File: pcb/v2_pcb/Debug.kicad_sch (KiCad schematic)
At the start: 2 parts, among them J1 Conn_ARM_SWD_TagConnect_TC203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

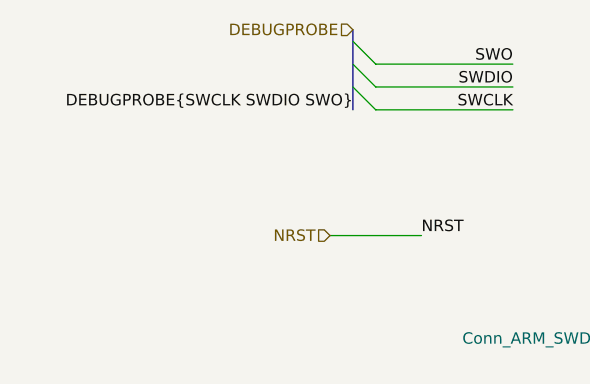
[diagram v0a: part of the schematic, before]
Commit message: done with max17320
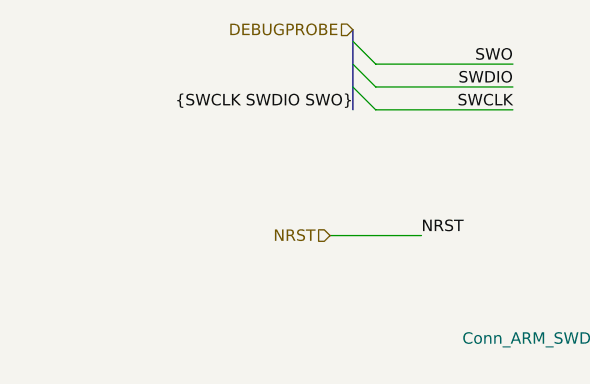
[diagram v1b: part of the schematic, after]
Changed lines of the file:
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@@
 		)
 	)
-	(label "DEBUGPROBE{SWCLK SWDIO SWO}"
+	(label "{SWCLK SWDIO SWO}"
 		(at 91.44 73.66 180)
 		(effects

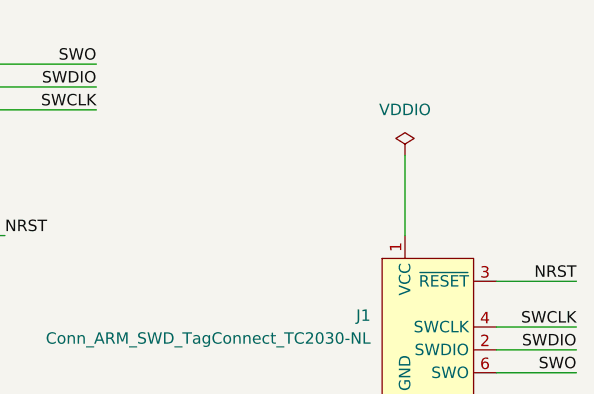
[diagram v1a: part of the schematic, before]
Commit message: add rpls for 1v8, 5v
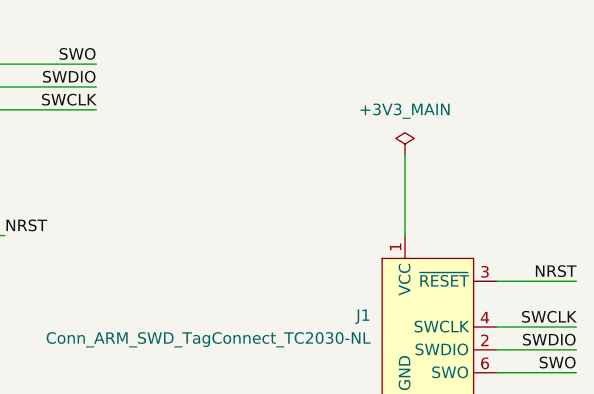
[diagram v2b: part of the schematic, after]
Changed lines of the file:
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@@
 			)
 		)
-		(property "Value" "VDDIO"
+		(property "Value" "+3V3_MAIN"
 			(at 143.51 73.66 0)
 			(show_name no)

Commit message: pcb done
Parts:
- added R327: 10k, Resistor_SMD:R_0402_1005Metric, symbol Device:R_Small_US
- added SW301: DEV BOOT, Button_Switch_SMD:SW_Push_1P1T_NO_CK_KMR2, symbol Switch:SW_Push
- added TP300: DEV_BOOT, TestPoint:TestPoint_Plated_Hole_D2.0mm, symbol Connector:TestPoint
- C1: footprint (none) -> Capacitor_SMD:C_0402_1005Metric
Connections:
- net GND: now also J1.5 (GND), R327.2
- net +3V3_MAIN: now reaches C1.1
- net +3V3_MAIN: now also J1.1 (VCC), SW301.1; no longer J1.5 (GND)
- new net DEV_BOOT: R327.1, SW301.2, TP300.1
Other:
- note added: "BOOT1 / DEV_BOOT (MCU PA6/P8) is sampled during reset; assert high only for development boot."
- note added: "Boot truth table (AN5967 Rev.4): BOOT1=1: development boot (BOOT0 ignored) BOOT1=0, BOOT0=0: Flash-memory boot BOOT1=0, BOOT0=1: serial boot"
- moved on the sheet: J1

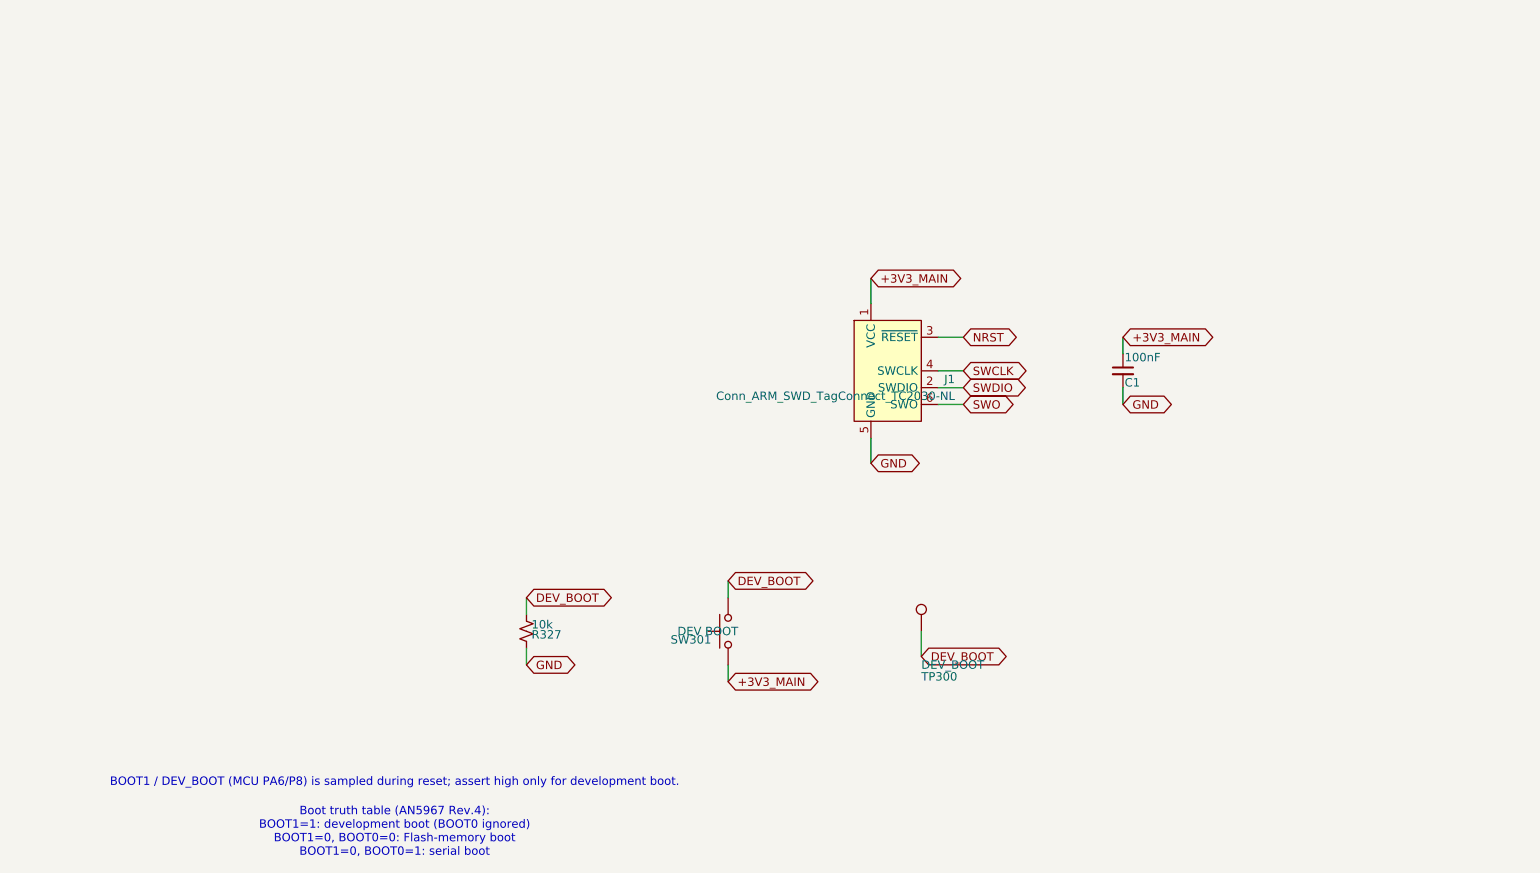
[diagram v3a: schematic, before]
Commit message: switch mosfets
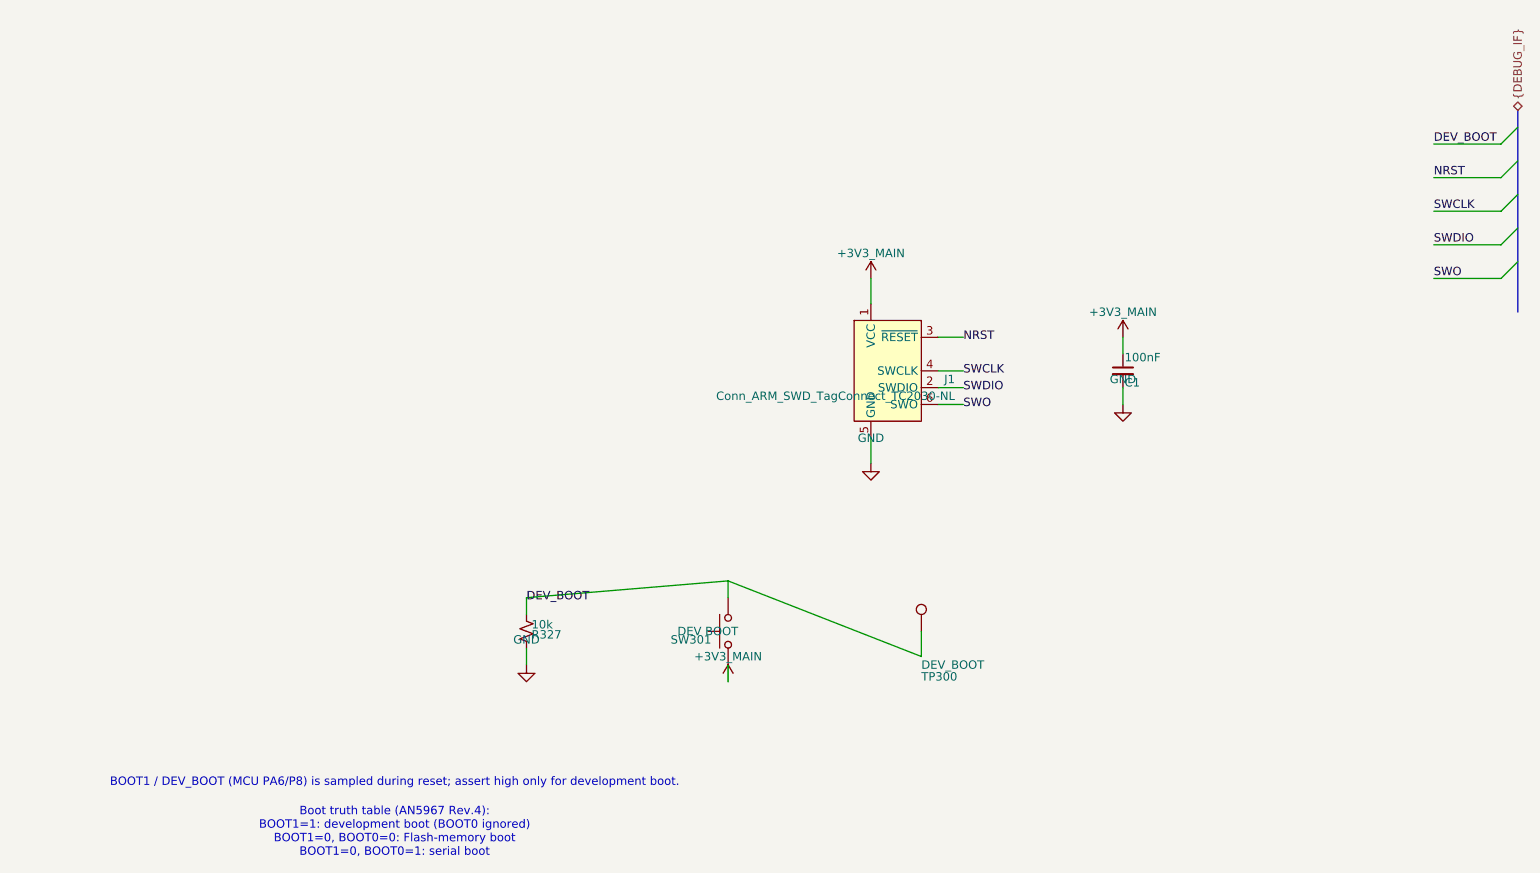
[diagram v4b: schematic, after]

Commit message: power and debug cleanup
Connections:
- net +3V3_MAIN: now also SW301.2; no longer SW301.1
- net DEV_BOOT: now also SW301.1; no longer SW301.2
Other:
- moved on the sheet: C1, R327, SW301, TP300

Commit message: minor fixes
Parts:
- C1: value 100nF -> 100nF 50V X7R; Dielectric (none) -> X7R; MPN (none) -> CGA2B3X7R1H104K050BE; Manufacturer (none) -> TDK; Qualification (none) -> AEC-Q200; Termination (none) -> Soft termination; Tolerance (none) -> ±10%; Voltage (none) -> 50 VDC
- R327: MPN RC0402FR-0710KL -> CRCW040210K0FKED; Manufacturer Yageo -> Vishay; Power (none) -> 0.063 W; Qualification (none) -> AEC-Q200; TCR (none) -> ±100 ppm/K; Tolerance (none) -> ±1%
- SW301: value DEV BOOT -> KMR223NG ULC LFG; Contact (none) -> Gold ULC; 1 µA minimum at 1.8 V; MPN KMR221GLFS -> Y78B22324FP; Manufacturer C&K -> Littelfuse (C&K); Operating_Temperature (none) -> -40 to +125 °C
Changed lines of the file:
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@@
 		)
 	)
-	(label "NRST"
+	(global_label "NRST"
 		(at 212.09 66.04 0)
 		(effects
@@
 		)
 	)
-	(label "NRST"
+	(global_label "NRST"
 		(at 140.97 90.17 0)
 		(effects
@@
 			)
 		)
-		(property "Value" "DEV BOOT"
+		(property "Value" "KMR223NG ULC LFG"
 			(at 120.65 123.19 0)
 			(show_name no)
@@
 			)
 		)
-		(property "Datasheet" ""
+		(property "Datasheet" "https://www.littelfuse.com/assetdocs/littelfuse-ck-tactile-kmr2-series-datasheet?assetguid=f782bfc7-b600-4ab5-8c8d-a2a094a642e3"
 			(at 120.65 127 0)
 			(show_name no)
@@
 			)
 		)
-		(property "MPN" "KMR221GLFS"
+		(property "MPN" "Y78B22324FP"
 			(at 123.19 132.0799 0)
 			(hide yes)
@@
 			)
 		)
-		(property "Manufacturer" "C&K"
+		(property "Manufacturer" "Littelfuse (C&K)"
 			(at 123.19 132.0799 0)
 			(hide yes)
@@
 			)
 		)
+    (property "Contact" "Gold ULC; 1 µA minimum at 1.8 V" (at 120.65 127.0 0)
+      (effects (font (size 1.27 1.27)) (hide yes))
+    )
+    (property "Operating_Temperature" "-40 to +125 °C" (at 120.65 127.0 0)
+      (effects (font (size 1.27 1.27)) (hide yes))
+    )
 		(pin "1"
 		)
@@
 		(in_bom no)
 		(on_board yes)
-		(in_pos_files yes)
+		(in_pos_files no)
 		(dnp no)
 		(property "Reference" "J1"
@@
 			)
 		)
-		(property "Datasheet" "https://www.yageo.com/upload/media/product/productsearch/datasheet/rchip/PYu-RC_Group_51_RoHS_L_12.pdf"
+		(property "Datasheet" "https://www.vishay.com/docs/20035/dcrcwe3.pdf"
 			(at 106.68 132.08 0)
 			(hide yes)
@@
 			)
 		)
-		(property "MPN" "RC0402FR-0710KL"
+		(property "MPN" "CRCW040210K0FKED"
 			(at 109.22 137.1599 0)
 			(hide yes)
@@
 			)
 		)
-		(property "Manufacturer" "Yageo"
+		(property "Manufacturer" "Vishay"
 			(at 109.22 137.1599 0)
 			(hide yes)
@@
 			)
 		)
+    (property "Tolerance" "±1%" (at 106.68 132.08 0)
+      (effects (font (size 1.27 1.27)) (hide yes))
+    )
+    (property "Power" "0.063 W" (at 106.68 132.08 0)
+      (effects (font (size 1.27 1.27)) (hide yes))
+    )
+    (property "TCR" "±100 ppm/K" (at 106.68 132.08 0)
+      (effects (font (size 1.27 1.27)) (hide yes))
+    )
+    (property "Qualification" "AEC-Q200" (at 106.68 132.08 0)
+      (effects (font (size 1.27 1.27)) (hide yes))
+    )
 		(pin "1"
 		)
@@
 			)
 		)
-		(property "Value" "100nF"
+		(property "Value" "100nF 50V X7R"
 			(at 120.65 96.52 0)
 			(show_name no)
@@
 			)
 		)
-		(property "Datasheet" ""
+		(property "Datasheet" "https://product.tdk.com/en/search/capacitor/ceramic/mlcc/info?part_no=CGA2B3X7R1H104K050BE"
 			(at 116.84 95.25 0)
 			(show_name no)
@@
 			)
 		)
+    (property "Manufacturer" "TDK" (at 116.84 95.25 0)
+      (effects (font (size 1.27 1.27)) (hide yes))
+    )
+    (property "MPN" "CGA2B3X7R1H104K050BE" (at 116.84 95.25 0)
+      (effects (font (size 1.27 1.27)) (hide yes))
+    )
+    (property "Voltage" "50 VDC" (at 116.84 95.25 0)
+      (effects (font (size 1.27 1.27)) (hide yes))
+    )
+    (property "Tolerance" "±10%" (at 116.84 95.25 0)
+      (effects (font (size 1.27 1.27)) (hide yes))
+    )
+    (property "Dielectric" "X7R" (at 116.84 95.25 0)
+      (effects (font (size 1.27 1.27)) (hide yes))
+    )
+    (property "Qualification" "AEC-Q200" (at 116.84 95.25 0)
+      (effects (font (size 1.27 1.27)) (hide yes))
+    )
+    (property "Termination" "Soft termination" (at 116.84 95.25 0)
+      (effects (font (size 1.27 1.27)) (hide yes))
+    )
 		(pin "1"
 		)
@@
 		(in_bom no)
 		(on_board yes)
-		(in_pos_files yes)
+		(in_pos_files no)
 		(dnp no)
 		(property "Reference" "TP300"
